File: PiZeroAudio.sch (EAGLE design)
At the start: 53 parts, among them CN1 1X4-BIG, CON1 RPI-ZERO, J1 1X2-3.5MM, U3 NC7WZ16, U4 TPA3144D2PWPR

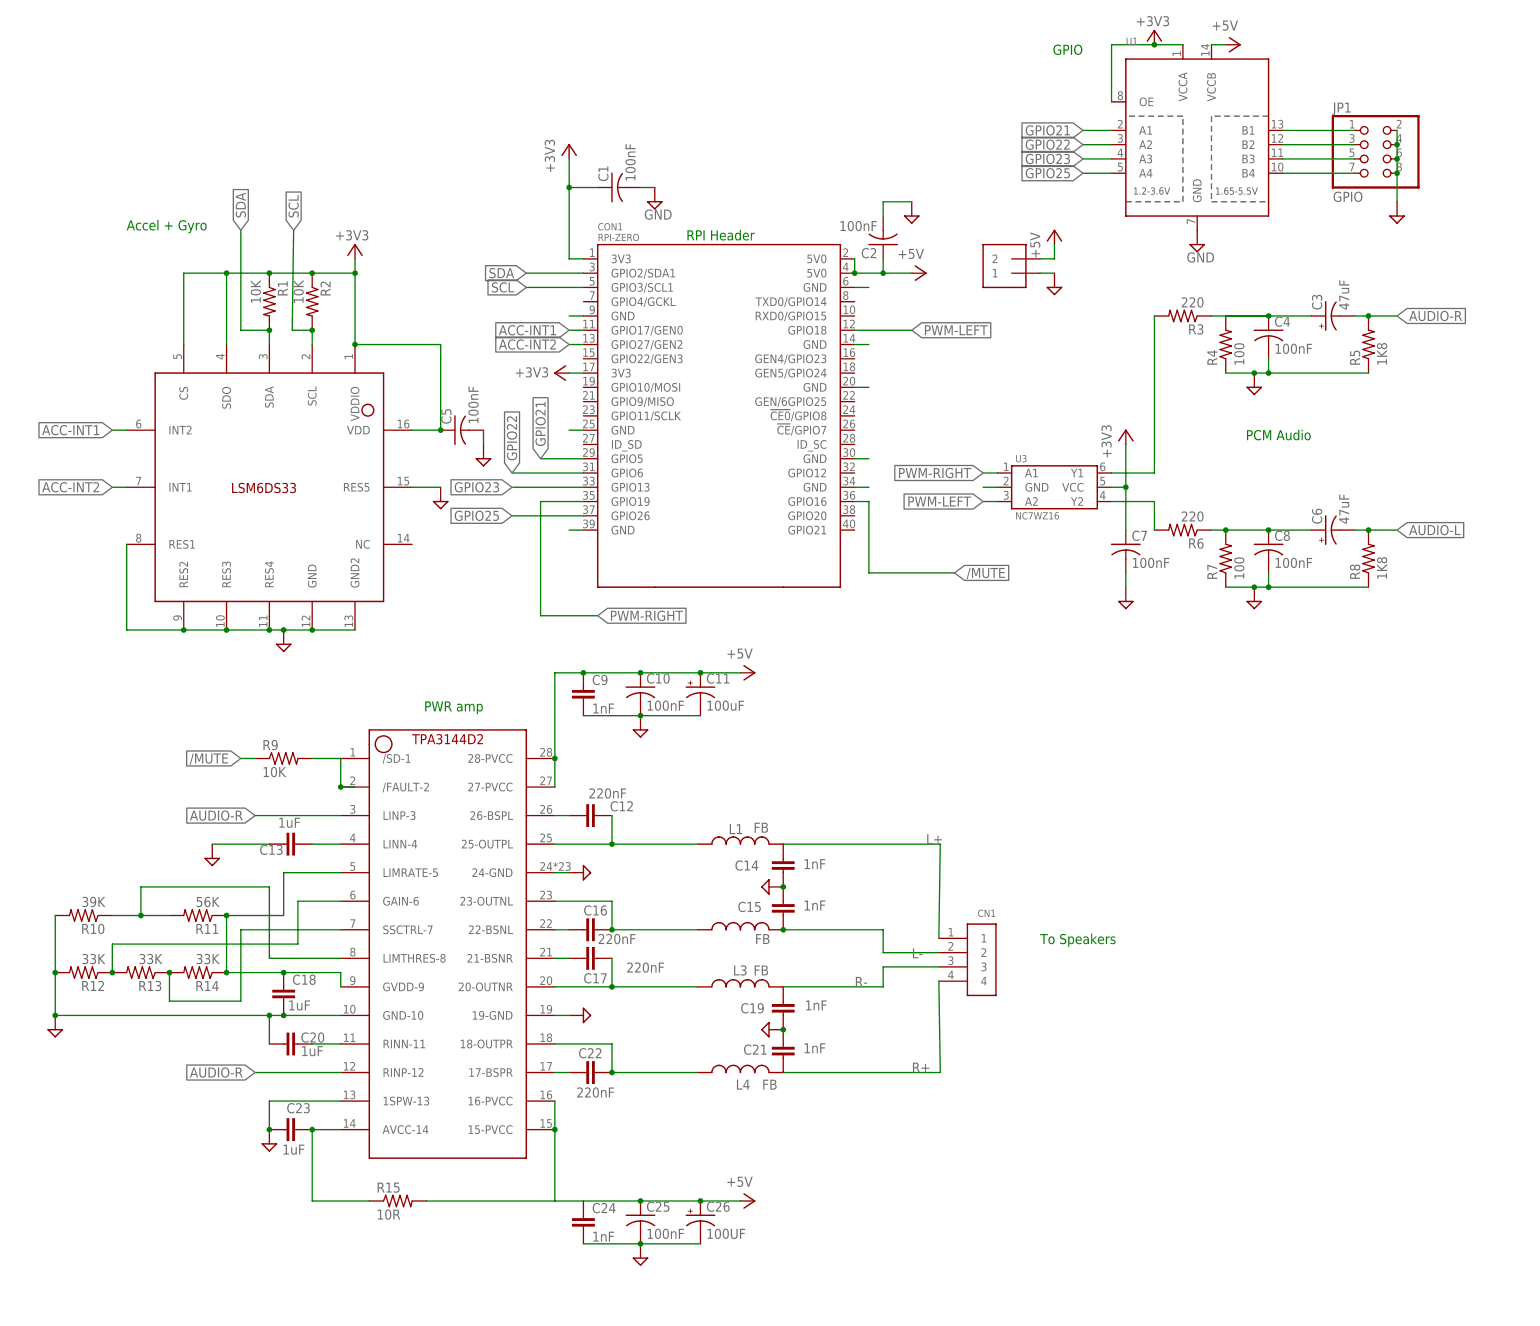
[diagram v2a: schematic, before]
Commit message: Consistency put back Removed GND pour from top
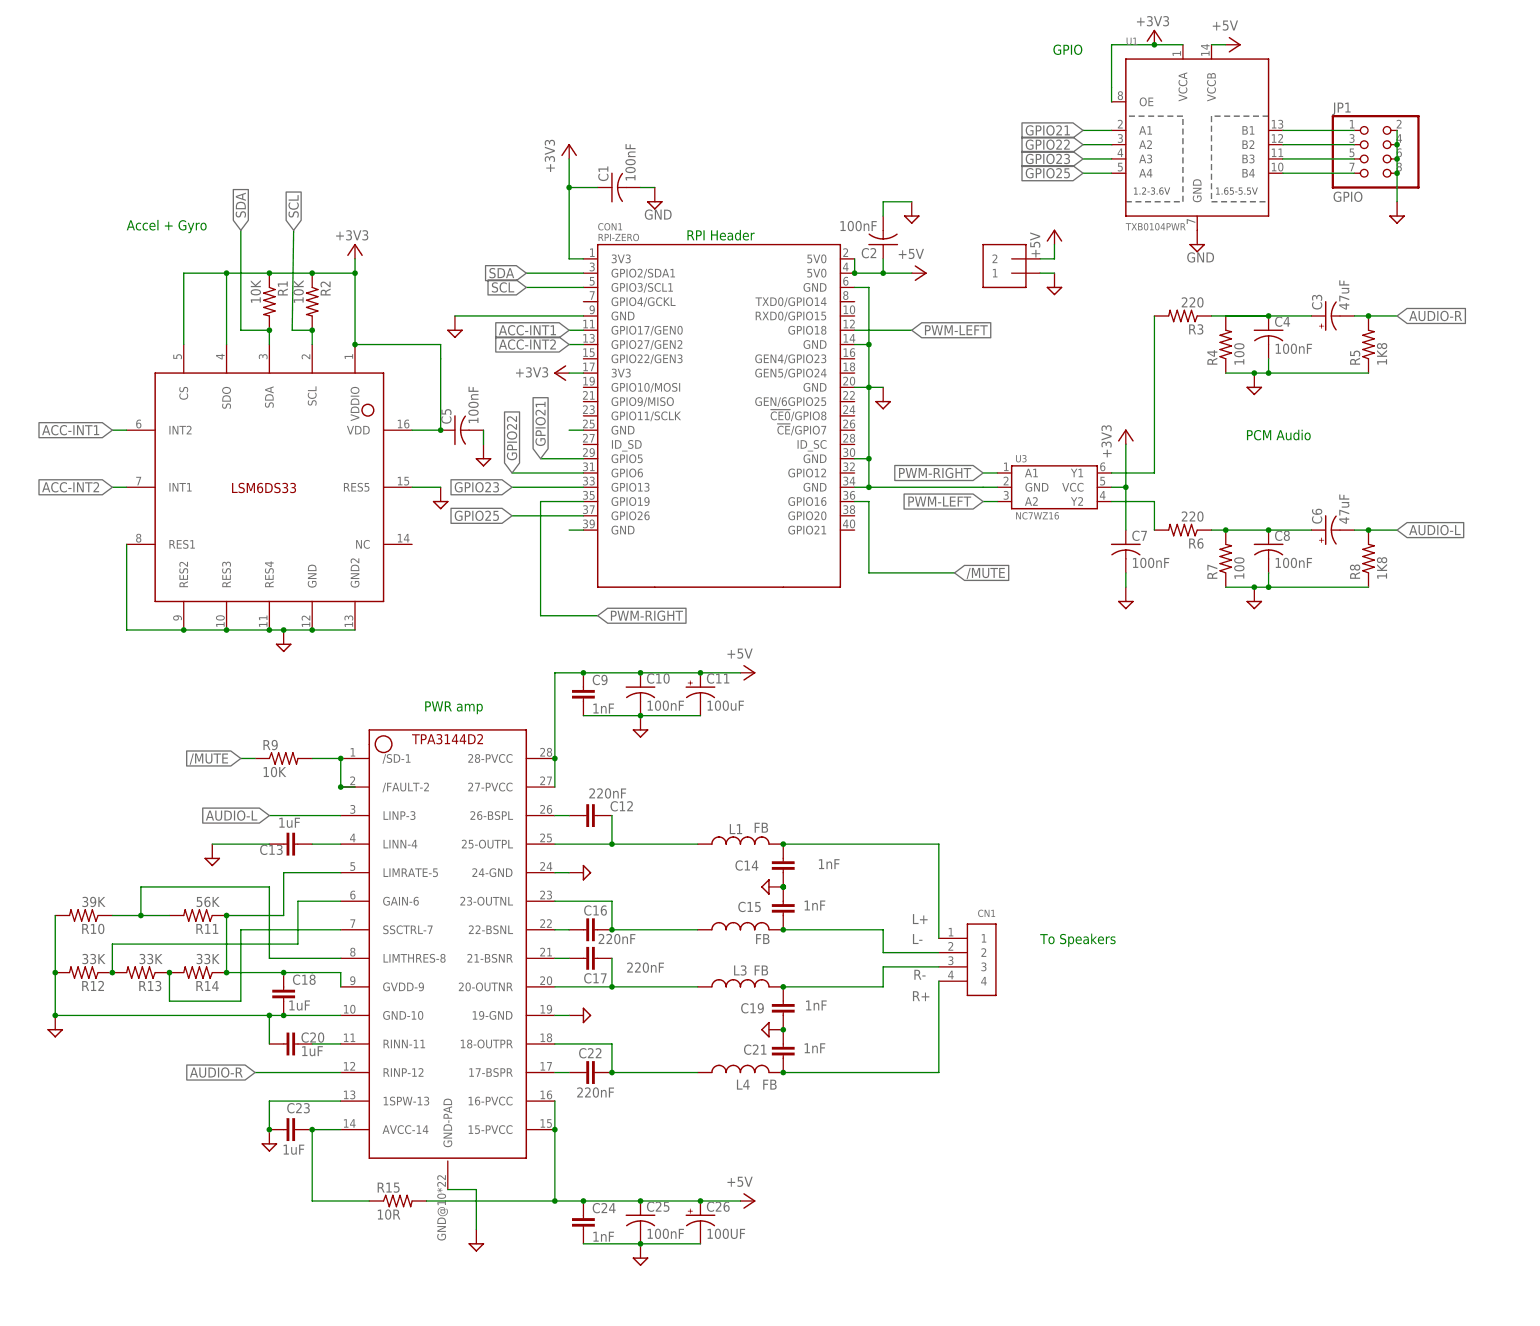
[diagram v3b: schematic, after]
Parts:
- U1: value (none) -> TXB0104PWR
- U2: value (none) -> LSM6DS33
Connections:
- removed net N$6: U4.LINP-3
- net AUDIO-L: now also U4.LINP-3
- net GND: now also U4.GND-PAD
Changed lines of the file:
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@@
 <part name="R5" library="adafruit" deviceset="R-US_" device="R0805" value="1K8"/>
 <part name="R8" library="adafruit" deviceset="R-US_" device="R0805" value="1K8"/>
-<part name="U2" library="HappyBrackets" library_urn="urn:adsk.eagle:library:5224691" deviceset="LSM6DS33" device="LGA-16-3X3" package3d_urn="urn:adsk.eagle:package:5224694/1"/>
+<part name="U2" library="HappyBrackets" library_urn="urn:adsk.eagle:library:5224691" deviceset="LSM6DS33" device="LGA-16-3X3" package3d_urn="urn:adsk.eagle:package:5224694/1" value="LSM6DS33"/>
 <part name="C5" library="adafruit" deviceset="C-US" device="C0805" value="100nF"/>
 <part name="+3V33" library="supply1" library_urn="urn:adsk.eagle:library:371" deviceset="+3V3" device=""/>
@@
 <part name="C2" library="adafruit" deviceset="C-US" device="C0805" value="100nF"/>
 <part name="SUPPLY2" library="supply2" library_urn="urn:adsk.eagle:library:372" deviceset="GND" device=""/>
-<part name="U1" library="adafruit" deviceset="TXB0104PWR" device=""/>
+<part name="U1" library="adafruit" deviceset="TXB0104PWR" device="" value="TXB0104PWR"/>
 <part name="SUPPLY4" library="supply2" library_urn="urn:adsk.eagle:library:372" deviceset="GND" device=""/>
 <part name="P+1" library="supply1" library_urn="urn:adsk.eagle:library:371" deviceset="+5V" device=""/>
@@
 <part name="JP1" library="adafruit" deviceset="PINHD-2X4" device="" value="GPIO"/>
 <part name="SUPPLY3" library="supply2" library_urn="urn:adsk.eagle:library:372" deviceset="GND" device=""/>
+<part name="SUPPLY21" library="supply2" library_urn="urn:adsk.eagle:library:372" deviceset="GND" device=""/>
+<part name="SUPPLY22" library="supply2" library_urn="urn:adsk.eagle:library:372" deviceset="GND" device=""/>
+<part name="SUPPLY23" library="supply2" library_urn="urn:adsk.eagle:library:372" deviceset="GND" device=""/>
 </parts>
 <sheets>
@@
 <instance part="C14" gate="G$1" x="-353.06" y="91.44" smashed="yes">
 <attribute name="NAME" x="-361.696" y="89.281" size="1.778" layer="95"/>
-<attribute name="VALUE" x="-349.504" y="89.535" size="1.778" layer="96"/>
+<attribute name="VALUE" x="-346.964" y="89.535" size="1.778" layer="96"/>
 </instance>
 <instance part="C15" gate="G$1" x="-353.06" y="83.82" smashed="yes">
@@
 <instance part="JP1" gate="A" x="-248.92" y="215.9"/>
 <instance part="SUPPLY3" gate="GND" x="-243.84" y="205.74" smashed="yes"/>
+<instance part="SUPPLY21" gate="GND" x="-407.67" y="22.86" smashed="yes"/>
+<instance part="SUPPLY22" gate="GND" x="-335.28" y="172.72" smashed="yes"/>
+<instance part="SUPPLY23" gate="GND" x="-411.48" y="185.42" smashed="yes"/>
 </instances>
 <busses>
@@
 <pinref part="CON1" gate="G$1" pin="GND@8"/>
 <wire x1="-340.36" y1="193.04" x2="-337.82" y2="193.04" width="0.1524" layer="91"/>
-</segment>
-<segment>
 <pinref part="CON1" gate="G$1" pin="GND@4"/>
 <wire x1="-340.36" y1="182.88" x2="-337.82" y2="182.88" width="0.1524" layer="91"/>
-</segment>
-<segment>
 <pinref part="CON1" gate="G$1" pin="GND@5"/>
 <wire x1="-340.36" y1="175.26" x2="-337.82" y2="175.26" width="0.1524" layer="91"/>
-</segment>
-<segment>
+<wire x1="-337.82" y1="182.88" x2="-337.82" y2="175.26" width="0.1524" layer="91"/>
 <pinref part="CON1" gate="G$1" pin="GND@6"/>
 <wire x1="-340.36" y1="162.56" x2="-337.82" y2="162.56" width="0.1524" layer="91"/>
-</segment>
-<segment>
 <pinref part="CON1" gate="G$1" pin="GND@7"/>
 <wire x1="-340.36" y1="157.48" x2="-337.82" y2="157.48" width="0.1524" layer="91"/>
+<pinref part="U3" gate="G$1" pin="GND"/>
+<wire x1="-314.96" y1="157.48" x2="-317.5" y2="157.48" width="0.1524" layer="91"/>
+<wire x1="-337.82" y1="157.48" x2="-317.5" y2="157.48" width="0.1524" layer="91"/>
+<wire x1="-337.82" y1="162.56" x2="-337.82" y2="157.48" width="0.1524" layer="91"/>
+<junction x="-337.82" y="157.48"/>
+<wire x1="-337.82" y1="175.26" x2="-337.82" y2="162.56" width="0.1524" layer="91"/>
+<junction x="-337.82" y="175.26"/>
+<junction x="-337.82" y="162.56"/>
+<wire x1="-337.82" y1="175.26" x2="-335.28" y2="175.26" width="0.1524" layer="91"/>
+<pinref part="SUPPLY22" gate="GND" pin="GND"/>
+<wire x1="-337.82" y1="193.04" x2="-337.82" y2="182.88" width="0.1524" layer="91"/>
+<junction x="-337.82" y="182.88"/>
 </segment>
 <segment>
@@
 <segment>
 <pinref part="CON1" gate="G$1" pin="GND@1"/>
-<wire x1="-388.62" y1="187.96" x2="-391.16" y2="187.96" width="0.1524" layer="91"/>
-</segment>
-<segment>
-<pinref part="U3" gate="G$1" pin="GND"/>
-<wire x1="-314.96" y1="157.48" x2="-317.5" y2="157.48" width="0.1524" layer="91"/>
+<wire x1="-388.62" y1="187.96" x2="-411.48" y2="187.96" width="0.1524" layer="91"/>
+<pinref part="SUPPLY23" gate="GND" pin="GND"/>
 </segment>
 <segment>
@@
 <pinref part="SUPPLY15" gate="GND" pin="GND"/>
 <junction x="-353.06" y="86.36"/>
+<junction x="-353.06" y="86.36"/>
 </segment>
 <segment>
@@
 <wire x1="-243.84" y1="213.36" x2="-243.84" y2="208.28" width="0.1524" layer="91"/>
 <junction x="-243.84" y="213.36"/>
+</segment>
+<segment>
+<pinref part="U4" gate="G$1" pin="GND-PAD"/>
+<pinref part="SUPPLY21" gate="GND" pin="GND"/>
+<wire x1="-412.75" y1="32.512" x2="-407.67" y2="32.512" width="0.1524" layer="91"/>
+<wire x1="-407.67" y1="32.512" x2="-407.67" y2="25.4" width="0.1524" layer="91"/>
 </segment>
 </net>
@@
 <junction x="-393.7" y="43.18"/>
 <wire x1="-393.7" y1="30.48" x2="-388.62" y2="30.48" width="0.1524" layer="91"/>
+<junction x="-388.62" y="30.48"/>
+<junction x="-393.7" y="30.48"/>
 </segment>
 </net>
@@
 <wire x1="-248.92" y1="187.96" x2="-243.84" y2="187.96" width="0.1524" layer="91"/>
 <junction x="-248.92" y="187.96"/>
-<label x="-447.04" y="99.06" size="1.778" layer="95" rot="R180" xref="yes"/>
 </segment>
 </net>
@@
 <pinref part="U4" gate="G$1" pin="/FAULT-2"/>
 <junction x="-431.8" y="104.14"/>
+<junction x="-431.8" y="109.22"/>
 </segment>
 </net>
@@
 <wire x1="-337.82" y1="142.24" x2="-322.58" y2="142.24" width="0.1524" layer="91"/>
 <label x="-322.58" y="142.24" size="1.778" layer="95" xref="yes"/>
-</segment>
-</net>
-<net name="N$6" class="0">
-<segment>
-<pinref part="U4" gate="G$1" pin="LINP-3"/>
-<wire x1="-447.04" y1="99.06" x2="-431.8" y2="99.06" width="0.1524" layer="91"/>
 </segment>
 </net>
@@
 <pinref part="CN1" gate="G$1" pin="2"/>
 <wire x1="-335.28" y1="74.676" x2="-325.374" y2="74.676" width="0.1524" layer="91"/>
-<label x="-330.2" y="73.66" size="1.778" layer="95"/>
+<label x="-330.2" y="76.2" size="1.778" layer="95"/>
 </segment>
 </net>
@@
 <pinref part="C14" gate="G$1" pin="1"/>
 <pinref part="L1" gate="G$1" pin="2"/>
-<wire x1="-353.06" y1="93.98" x2="-325.12" y2="93.98" width="0.1524" layer="91"/>
+<wire x1="-353.06" y1="93.98" x2="-325.374" y2="93.98" width="0.1524" layer="91"/>
 <pinref part="CN1" gate="G$1" pin="1"/>
-<wire x1="-325.12" y1="93.98" x2="-325.374" y2="77.216" width="0.1524" layer="91"/>
-<label x="-327.66" y="93.98" size="1.778" layer="95"/>
+<wire x1="-325.374" y1="93.98" x2="-325.374" y2="77.216" width="0.1524" layer="91"/>
+<label x="-330.2" y="79.756" size="1.778" layer="95"/>
+<junction x="-353.06" y="93.98"/>
 </segment>
 </net>
@@
 <wire x1="-335.28" y1="72.136" x2="-335.28" y2="68.58" width="0.1524" layer="91"/>
 <wire x1="-335.28" y1="68.58" x2="-353.06" y2="68.58" width="0.1524" layer="91"/>
-<label x="-340.36" y="68.58" size="1.778" layer="95"/>
+<label x="-329.946" y="69.85" size="1.778" layer="95"/>
+<junction x="-353.06" y="68.58"/>
 </segment>
 </net>
@@
 <pinref part="C21" gate="G$1" pin="2"/>
 <pinref part="L4" gate="G$1" pin="2"/>
-<wire x1="-353.06" y1="53.34" x2="-325.12" y2="53.34" width="0.1524" layer="91"/>
+<wire x1="-353.06" y1="53.34" x2="-325.374" y2="53.34" width="0.1524" layer="91"/>
 <pinref part="CN1" gate="G$1" pin="4"/>
-<wire x1="-325.12" y1="53.34" x2="-325.374" y2="69.596" width="0.1524" layer="91"/>
-<label x="-330.2" y="53.34" size="1.778" layer="95"/>
+<wire x1="-325.374" y1="53.34" x2="-325.374" y2="69.596" width="0.1524" layer="91"/>
+<label x="-330.2" y="66.04" size="1.778" layer="95"/>
+<junction x="-353.06" y="53.34"/>
 </segment>
 </net>
@@
 <junction x="-248.92" y="149.86"/>
 </segment>
+<segment>
+<pinref part="U4" gate="G$1" pin="LINP-3"/>
+<wire x1="-431.8" y1="99.06" x2="-444.5" y2="99.06" width="0.1524" layer="91"/>
+<label x="-444.5" y="99.06" size="1.778" layer="95" rot="R180" xref="yes"/>
+</segment>
 </net>
 </nets>
 </sheet>
 </sheets>
+<errors>
+</errors>
 </schematic>
 </drawing>

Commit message: Applied star Power
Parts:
- added SH1, SH2: SHORT, HappyBrackets:SHORT
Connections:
- new net AGND: C10.2, C11.-, C13.2, C14.2, C15.1, C18.2, C19.2, C20.2, C21.1, C23.2, C24.2, C25.2, C26.-, C4.2, C7.2, C8.2, C9.2, J1.1, R10.2, R12.2, R4.1, R5.1, R7.1, R8.1, SH2.AN, U4.19-GND, U4.1SPW-13, U4.24-GND, U4.GND-10
- new net AN3V3: C7.1, SH1.AN, U3.VCC
- net +3V3: now also SH1.DIG; no longer C7.1, U3.VCC
- net GND: now also SH2.DIG; no longer C10.2, C11.-, C13.2, C14.2, C15.1, C18.2, C19.2, C20.2, C21.1, C23.2, C24.2, C25.2, C26.-, C4.2, C7.2, C8.2, C9.2, J1.1, R10.2, R12.2, R4.1, R5.1, R7.1, R8.1, U4.19-GND, U4.1SPW-13, U4.24-GND, U4.GND-10

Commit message: Changed Ferrite Beads
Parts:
- C1, C10, C2, C25, C4, C5, C7, C8: device adafruit:C-USC0805 -> rcl:C-EUC0603
- C12, C13, C14, C15, C16, C17, C18, C19, C20, C21, C22, C23, C24, C9: device resistor:C-EUC0805 -> rcl:C-EUC0603
- L1, L2, L3, L4: device HappyBrackets:BLM31A -> HappyBrackets:NFZ2MSML0806
- R1, R10, R11, R12, R13, R14, R15, R2, R3, R4, R5, R6, R7, R8, R9: device adafruit:R-US_R0805 -> adafruit:R-US_R0603
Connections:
- net AGND: now also U4.GND-PAD
- net GND: no longer U4.GND-PAD

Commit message: Routed all but power
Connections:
- net PWM-LEFT renamed PWM-R
- net PWM-RIGHT renamed PWM-L
- removed net AUDIO-L: C6.-, R8.2, U4.LINP-3
- removed net AUDIO-R: C3.-, R5.2, U4.RINP-12
- new net AUDIO-LEFT: C3.-, R5.2, U4.LINP-3
- new net AUDIO-RIGHT: C6.-, R8.2, U4.RINP-12
- net GPIO21: now also U1.A4; no longer U1.A1
- net GPIO22: now also U1.A3; no longer U1.A2
- net GPIO23: now also U1.A2; no longer U1.A3
- net GPIO25: now also U1.A1; no longer U1.A4

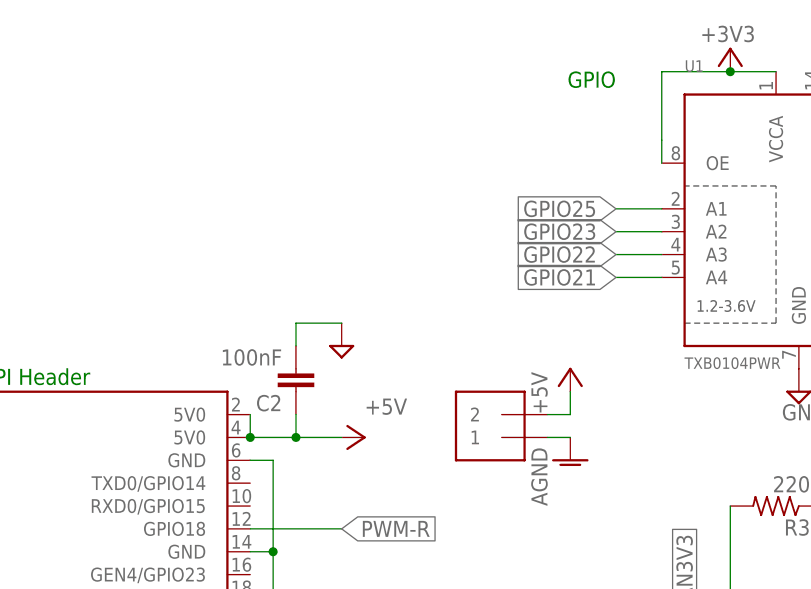
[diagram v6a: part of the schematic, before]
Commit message: Added LED
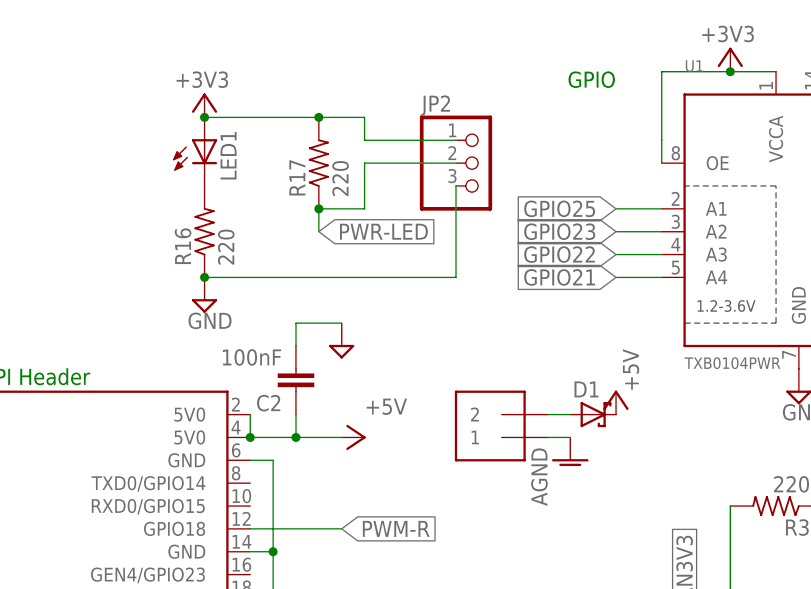
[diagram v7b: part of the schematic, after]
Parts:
- added D1: (no value), diode:SCHOTTKY-DIODESMD
- added JP2: (no value), adafruit:PINHD-1X3
- added LED1: (no value), adafruit:LEDCHIP-LED0805
- added R16, R17: 220, adafruit:R-US_R0603
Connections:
- new net N$6: LED1.C, R16.2
- new net PWR-IN: D1.A, J1.2
- new net PWR-LED: JP2.2, R17.1
- net +3V3: now also JP2.1, LED1.A, R17.2
- net +5V: now also D1.C; no longer J1.2
- net GND: now also JP2.3, R16.1
